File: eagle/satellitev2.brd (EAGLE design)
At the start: 43.2 x 41.4 mm, 9 parts, among them J1 RJ11-6PTH, U3 MAX3232PTH

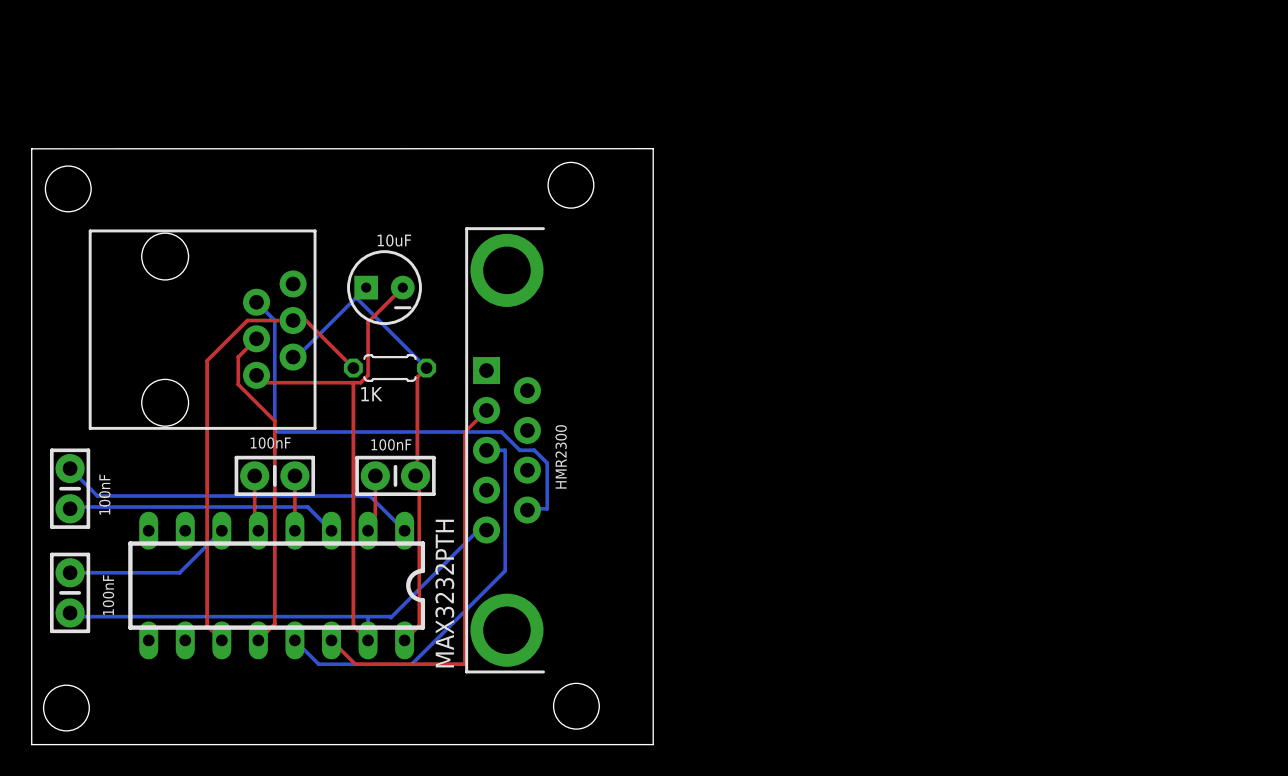
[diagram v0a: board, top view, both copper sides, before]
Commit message: added smaller satellite board
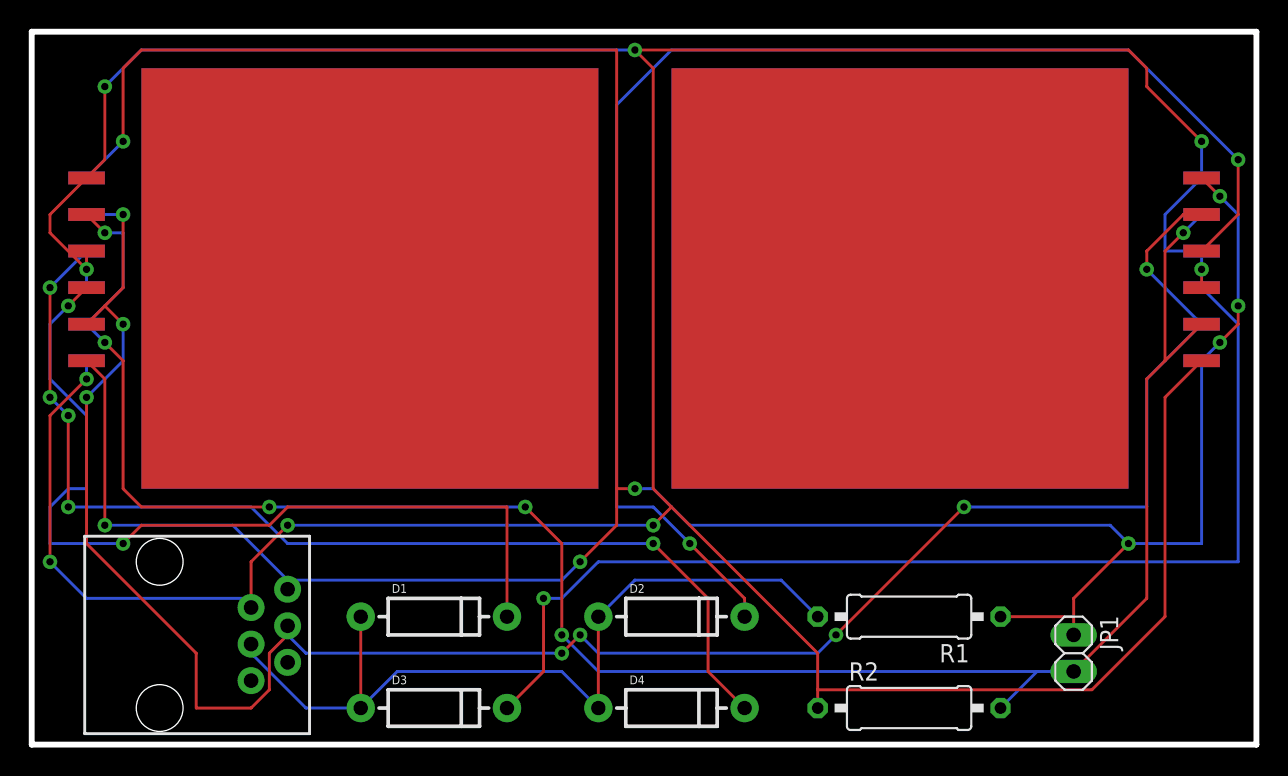
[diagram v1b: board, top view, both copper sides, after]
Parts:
- removed C2: 10uF, SparkFun-Capacitors:CPOL-RADIAL-10UF-25V
- removed C3, C4, C5, C6: 100nF, SparkFun-Capacitors:CAP-PTH-SMALL-KIT
- removed HMR2300: RS232, SparkFun-Connectors:DB9
- removed U3: MAX3232PTH, SparkFun-DigitalIC:DIL16
- added D1, D2, D3, D4: (no value), SparkFun-DiscreteSemi:DIODE-1N4001
- added JP1: (no value), pinhead:1X02
- added R2: 2.2K, rcl:0309/12
- added U$1, U$2: 1X6SMDPINS, 1x6smdpins:1X6SMDPINS
- added U$3, U$4: 1X6SMDPINSB, 1x6smdpins:1X6SMDPINSB
- R1: value 1K -> 2.2K; device rcl:0204/5 -> rcl:0309/12
- moved R1 40.0 mm to (61.0, 8.89), turned to 180 degrees
- moved J1 21.2 mm to (8.89, 12.7)
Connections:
- removed net 33V: C2.1, C4.1, J1.5, R1.2, U3.16
- removed net DI: J1.3, R1.1, U3.11
- removed net DO: J1.4, U3.12
- removed net N$12: C6.1, U3.6
- removed net N$5: C5.2, U3.5
- removed net N$8: C4.2, U3.2
- removed net RS232DI: HMR2300.3, U3.13
- removed net RS232DO: HMR2300.2, U3.14
- removed net VIN: HMR2300.9, J1.2
- new net 5V: J1.1, JP1.1, R1.1, U$1.P$6, U$2.P$1, U$3.P$6, U$4.P$1
- new net BR: JP1.2, R2.2, U$1.P$2, U$2.P$5, U$3.P$2, U$4.P$5
- new net N$1: D2.C, U$2.P$3
- new net RX: J1.3, U$1.P$5, U$2.P$2, U$3.P$5, U$4.P$2
- new net TX: D1.A, D2.A, D3.A, D4.A, J1.4, R1.2
- net GND: now also J1.2, R2.1, U$1.P$1, U$1.P$3, U$2.P$4, U$2.P$6, U$3.P$1, U$3.P$3, U$4.P$4, U$4.P$6; no longer C2.2, C6.2, HMR2300.5, J1.6, U3.15
- net N$2: now also D1.C, U$1.P$4; no longer C3.1, U3.1
- net N$3: now also D4.C, U$4.P$3; no longer C3.2, U3.3
- net N$4: now also D3.C, U$3.P$4; no longer C5.1, U3.4
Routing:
- net 5V: track 0.00 -> 210.5 mm, vias 0 -> 8
- net GND: track 67.1 -> 272.9 mm, vias 0 -> 9
- net RX: track 0.00 -> 146.4 mm, vias 0 -> 8
- net BR: track 0.00 -> 140.6 mm, vias 0 -> 6
- net N$1: track 0.00 -> 96.0 mm, vias 0 -> 2
- net N$4: track 3.81 -> 78.1 mm, vias 0 -> 1
- net TX: track 0.00 -> 58.5 mm
- net N$3: track 18.9 -> 75.1 mm, vias 0 -> 5
- net N$2: track 25.0 -> 62.1 mm, vias 0 -> 2
- net 33V: track 34.7 -> 0.00 mm
- net VIN: track 33.9 -> 0.00 mm
- net DI: track 32.5 -> 0.00 mm
- net RS232DO: track 28.2 -> 0.00 mm
- net RS232DI: track 27.6 -> 0.00 mm
- net DO: track 23.0 -> 0.00 mm
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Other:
- board size 43.2 x 41.4 mm -> 85.1 x 49.5 mm
- board text removed: "100nF"
- board text removed: "ADAM CHASE 08/13/13"
- board text removed: "TTL-RS232 v1.10"

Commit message: modified eagle files, should be ready to order
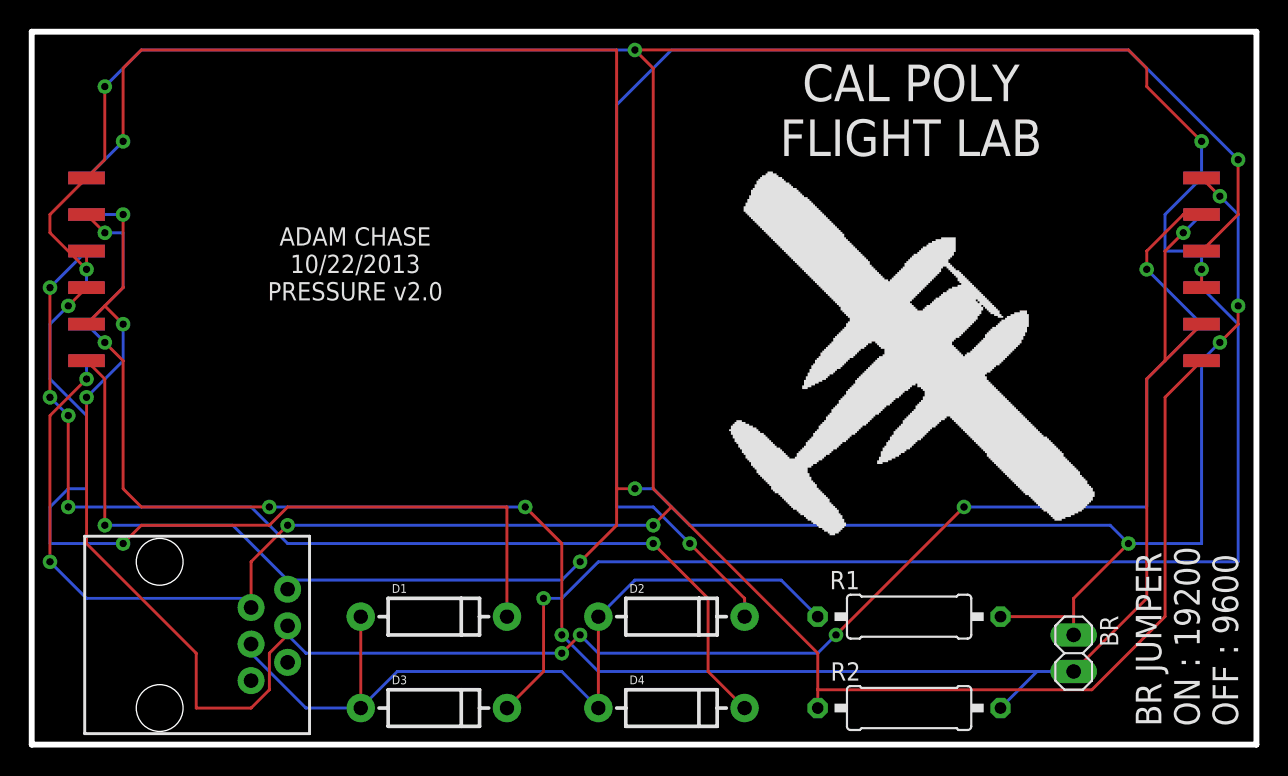
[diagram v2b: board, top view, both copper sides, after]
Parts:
- renumbered JP1 to BR
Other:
- board text added: "ADAM CHASE 10/22/2013 PRESSURE v2.0"
- board text added: "BR JUMPER ON : 19200 OFF : 9600"
- board text added: "CAL POLY FLIGHT LAB"
